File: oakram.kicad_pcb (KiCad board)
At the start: 2 copper layers, 42.5 x 54 mm, 20 parts, among them U1 IS41C16105C, U2 IS41C16105C, X1 ZIP40, X2 ZIP40

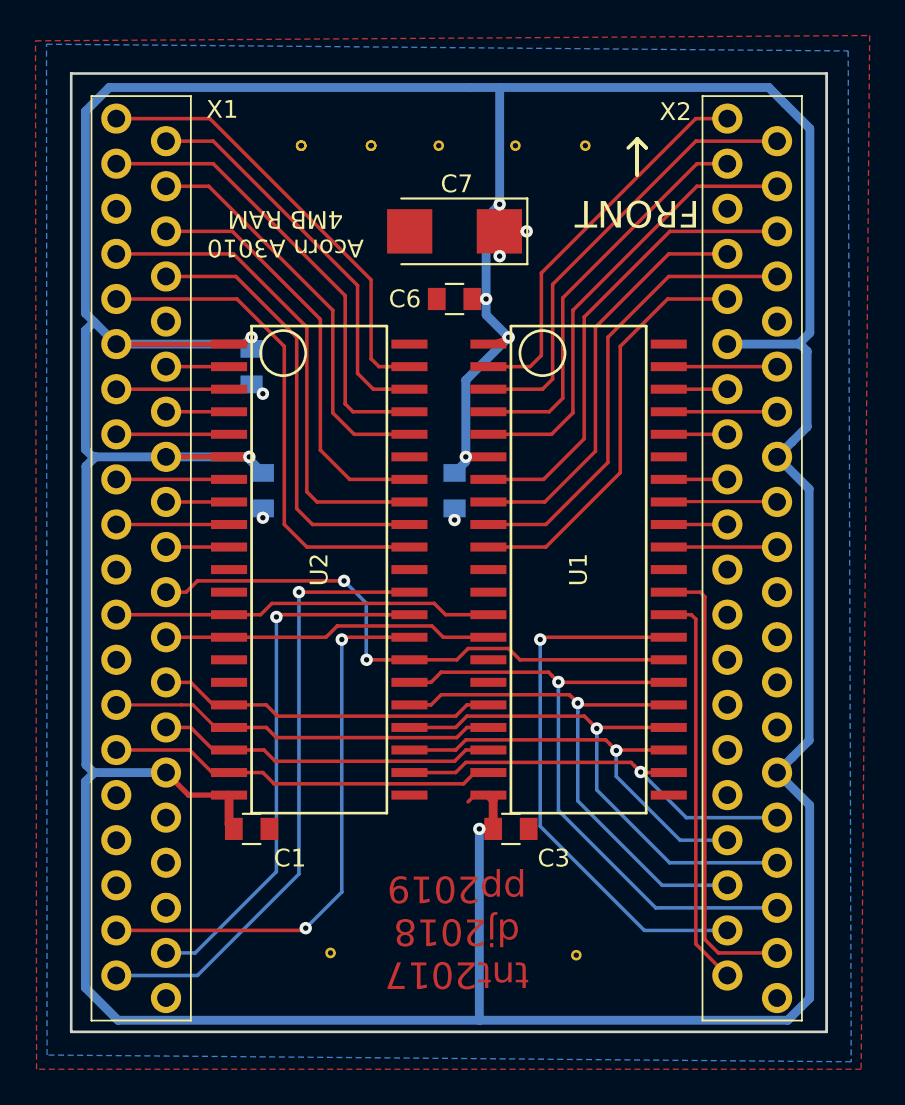
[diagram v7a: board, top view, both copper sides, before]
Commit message: Reduced hole and pad size on ZIP sockets, tightened top layer plane clearance to 6 mil, moved data lines to allow ground plane to pour between every pair
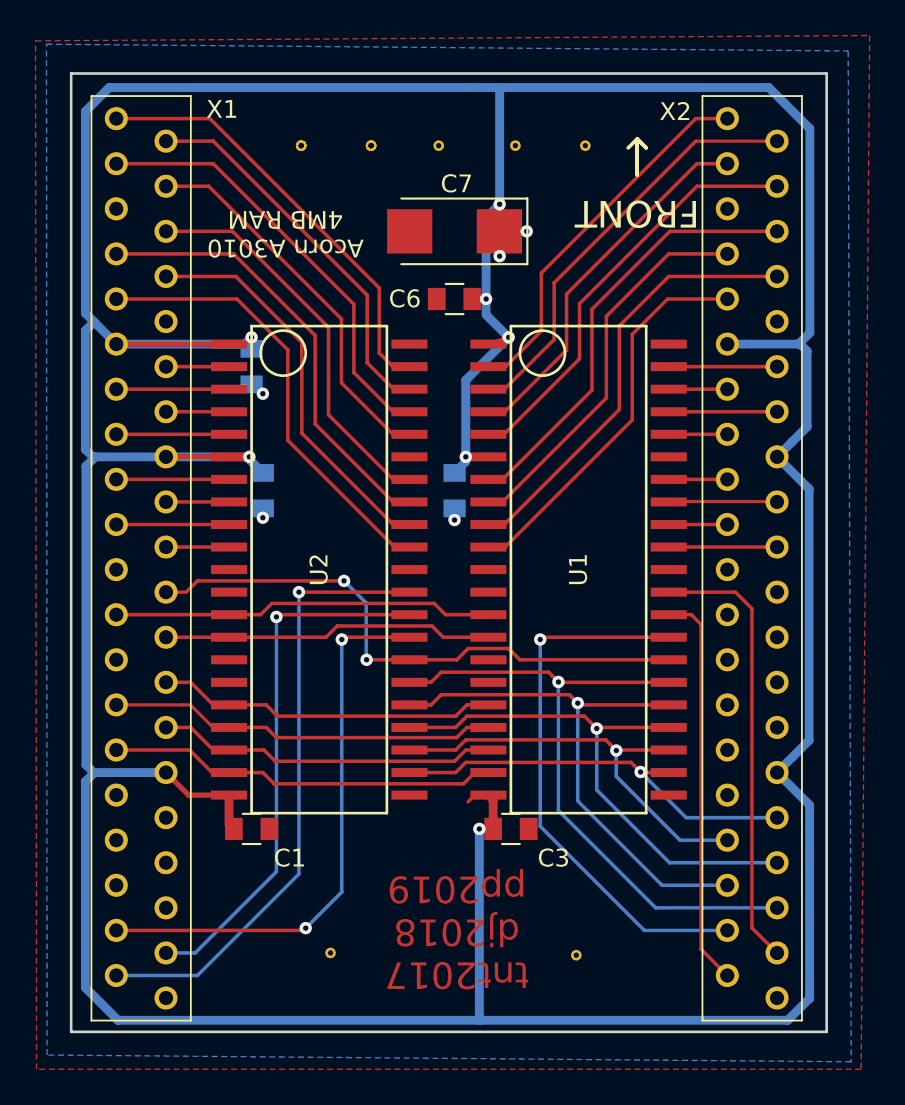
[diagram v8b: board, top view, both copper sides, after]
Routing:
- net /D15: track 28.2 -> 25.3 mm
- net /D14: track 25.2 -> 22.5 mm
- net /D13: track 27.7 -> 25.2 mm
- net /D27: track 25.4 -> 23.9 mm
- net /D26: track 22.6 -> 21.1 mm
- net /D12: track 23.8 -> 22.4 mm
- net /D29: track 23.3 -> 21.9 mm
- net /D30: track 26.2 -> 24.8 mm
- net /D28: track 26.1 -> 24.7 mm
- net /D31: track 23.4 -> 22.1 mm
- net /D10: track 25.9 -> 24.5 mm
- net /D11: track 22.9 -> 21.6 mm
- net /D25: track 25.2 -> 23.9 mm
- net /D24: track 22.0 -> 21.2 mm
- net /~CAS3: track 25.8 -> 25.0 mm
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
